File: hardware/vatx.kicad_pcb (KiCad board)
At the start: 2 copper layers, 50 x 50.1 mm, 27 parts, among them J1 USB, P1 CONN_10X2, P3 CONN_1, P4 CONN_1, P5 CONN_1, P6 CONN_1, P7 CONN_1, SW1 SWITCH_INV, U1 LM317T

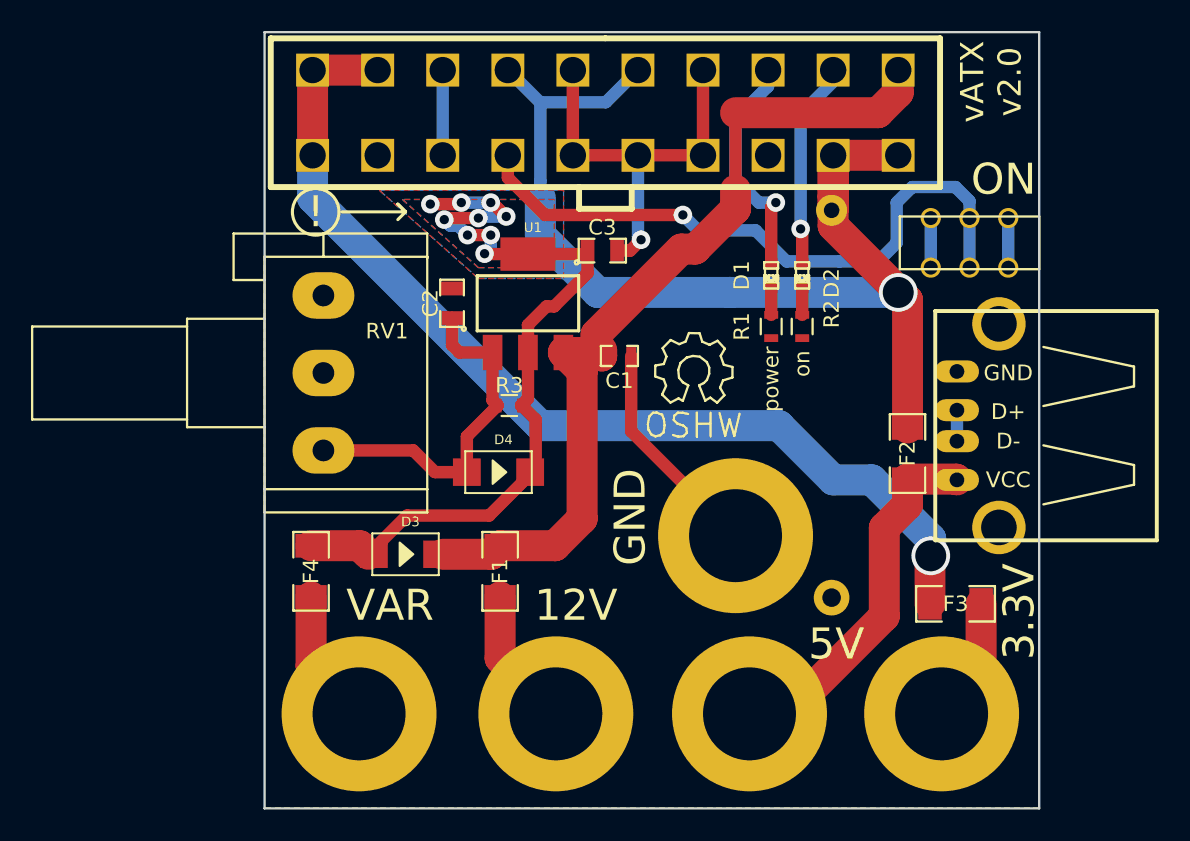
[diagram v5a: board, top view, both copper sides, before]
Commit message: Add pin-header for every voltage
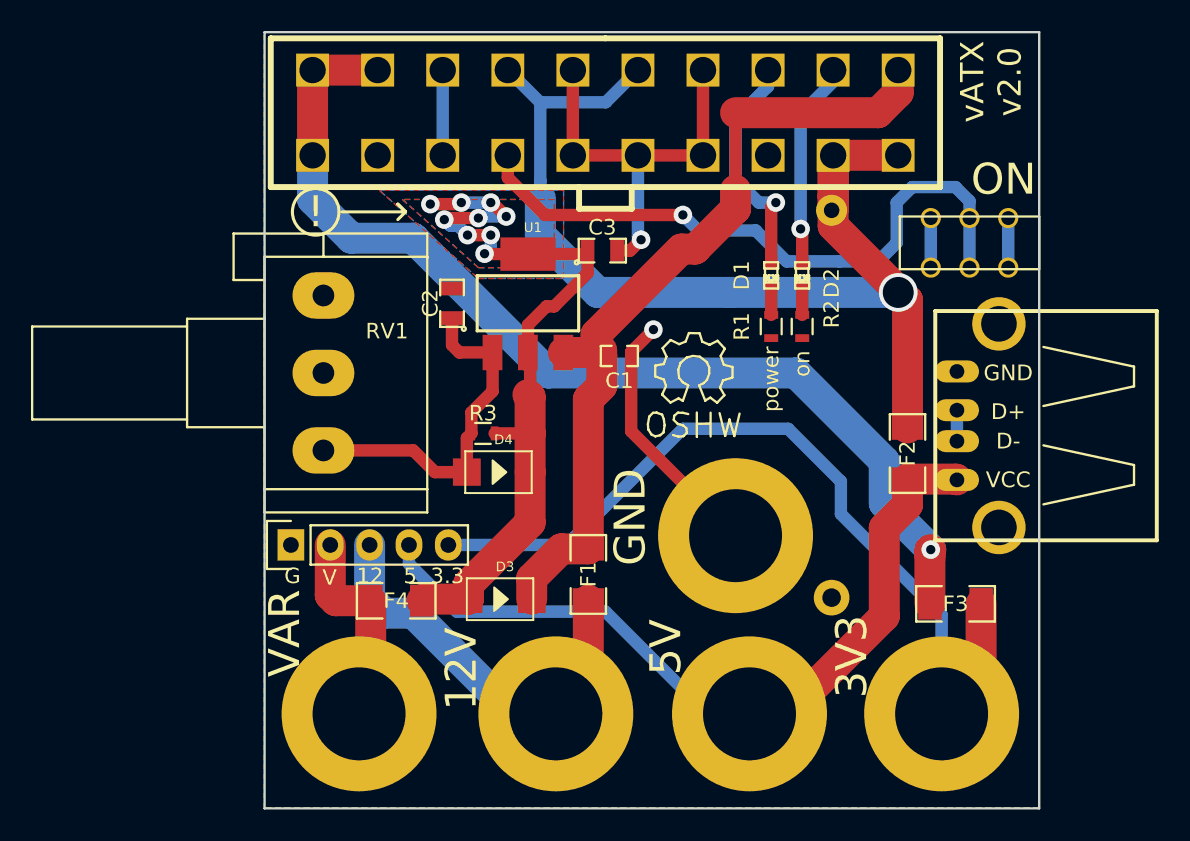
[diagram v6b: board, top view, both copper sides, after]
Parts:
- added P2: CONN_01X05, Pin_Headers:Pin_Header_Straight_1x05, F.Cu at (108.5, 82.7)
- D1: value LED -> blue
- D2: value LED -> yellow
- moved D3 6.75 mm to (122.0, 86.2)
- moved F4 5.82 mm to (115.3, 86.3), turned to 180 degrees
- moved F1 5.70 mm to (127.7, 84.6)
- moved R3 2.48 mm to (120.9, 75.5)
- moved Symbol_OSHW-Logo_SilkScreen_BIG 1.40 mm to (126.5, 50.5)
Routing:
- net f+3.3V: track 10.4 -> 57.9 mm
- net f+5V: track 24.0 -> 51.2 mm
- net f+12V: track 9.04 -> 26.8 mm
- net +12V: track 58.6 -> 55.3 mm
- net GND: track 49.9 -> 52.2 mm, vias 1 -> 2
- net +VAR: track 55.5 -> 53.5 mm
- net +3.3V: track 65.7 -> 66.9 mm
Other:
- board text added: "+12"
- board text added: "+3.3"
- board text added: "+5"
- board text added: "12"
- board text added: "3.3"
- board text added: "3V3"
- board text added: "5"
- board text added: "G"
- board text added: "Gnd"
- board text added: "V"
- board text added: "Var"
- board text removed: "3.3V"

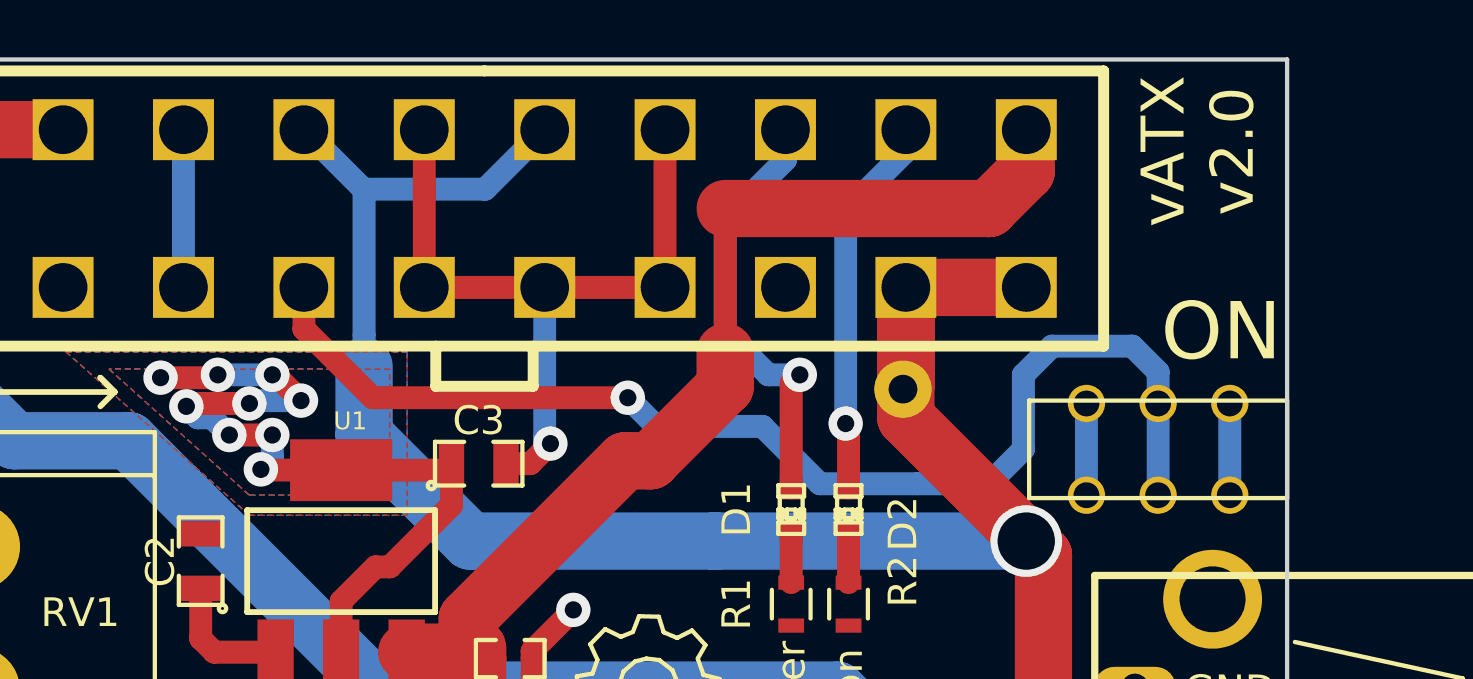
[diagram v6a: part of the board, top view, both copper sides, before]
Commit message: pcb for optional PSON control
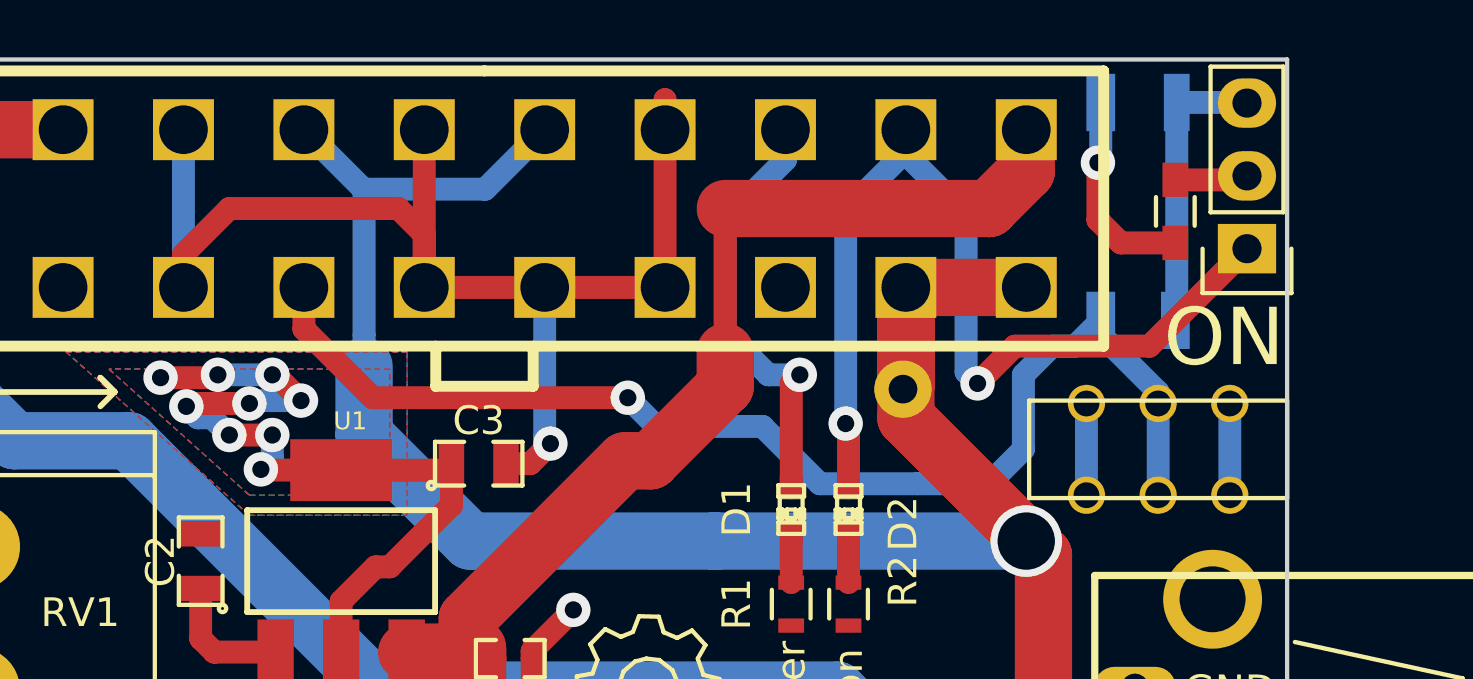
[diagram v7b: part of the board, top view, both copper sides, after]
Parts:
- added P8: CONN_01X03, Pin_Headers:Pin_Header_Straight_1x03, F.Cu at (155.4, 56.2)
- added R4: R, Resistors_SMD:R_0603_HandSoldering, F.Cu at (152.9, 54.9)
- added U2: OPTO-TRANSISTOR4, Opto-Devices:Optocoupler_SMD_HandSoldering_KPC357_LTV35x_PC357_SingleChannel, B.Cu at (151.6, 54.9)
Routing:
- net GND: track 52.2 -> 77.2 mm
- net +5VSB: track 13.4 -> 35.9 mm, vias 1 -> 2
- net Net-(R4-Pad2): track 0.00 -> 7.17 mm, vias 0 -> 1
- net Net-(P8-Pad2): track 0.00 -> 2.56 mm
- net PSON: track 41.7 -> 42.3 mm
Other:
- board text added: "vATX v2.1"
- board text removed: "vATX v2.0"

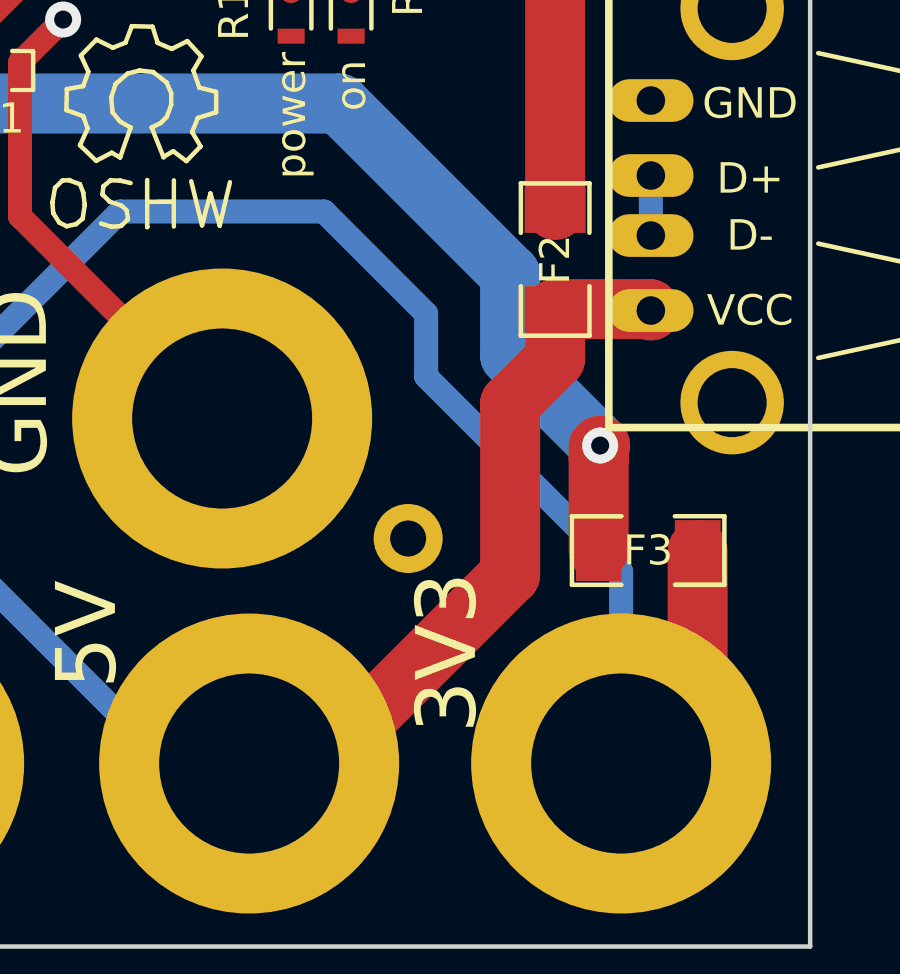
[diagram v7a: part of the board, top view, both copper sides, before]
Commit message: Remove fuse for 5V usb
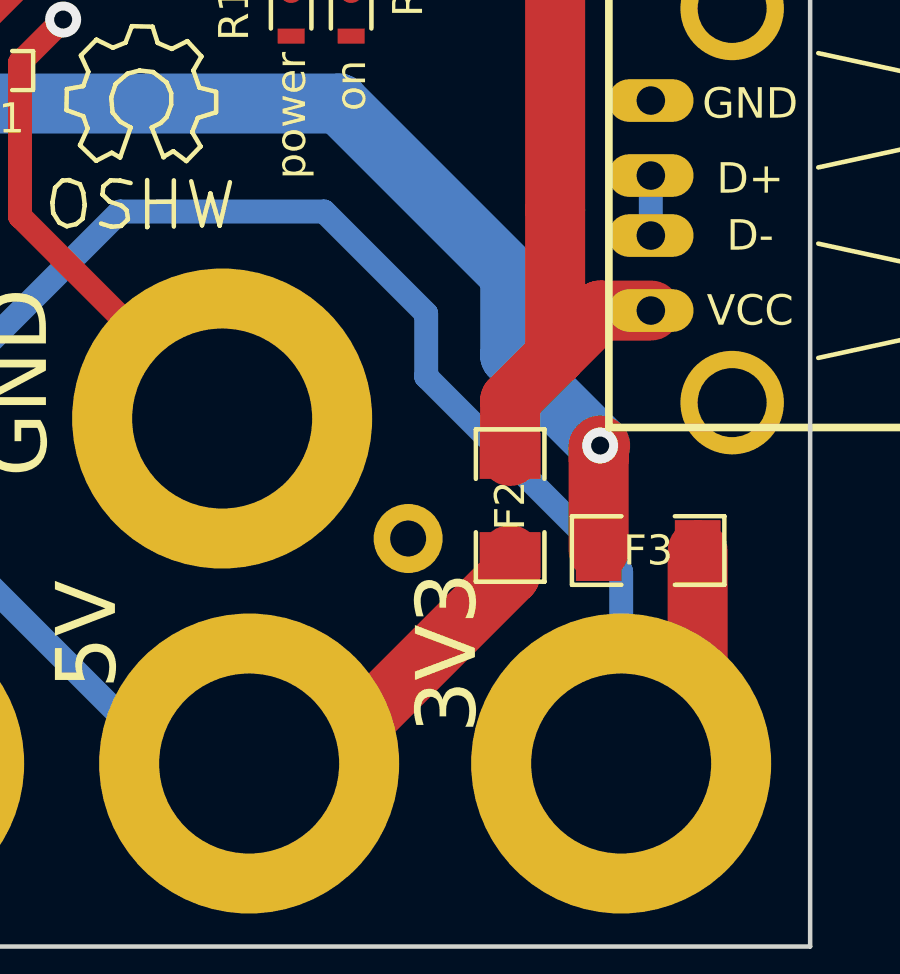
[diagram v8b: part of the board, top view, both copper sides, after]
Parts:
- moved F2 8.34 mm to (146.8, 85.0)
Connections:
- J1 pad 1: f+5V -> +5V
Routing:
- net +5V: track 71.6 -> 84.2 mm
- net f+5V: track 51.2 -> 41.6 mm
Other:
- board text added: "vATX v2.2"
- board text removed: "vATX v2.1"
